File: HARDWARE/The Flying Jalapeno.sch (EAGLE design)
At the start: 97 parts, among them Q2 MMBT2222A, Q3 NDP6020P, Q4 MMBT2222A, Q5 NDP6020P, Q6 BSS138, 200mA/50V, Q7 BSS138, 200mA/50V, U1 ATMEGA2560AU, U2 LM1117, U3 LM1117, U4 LM1117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

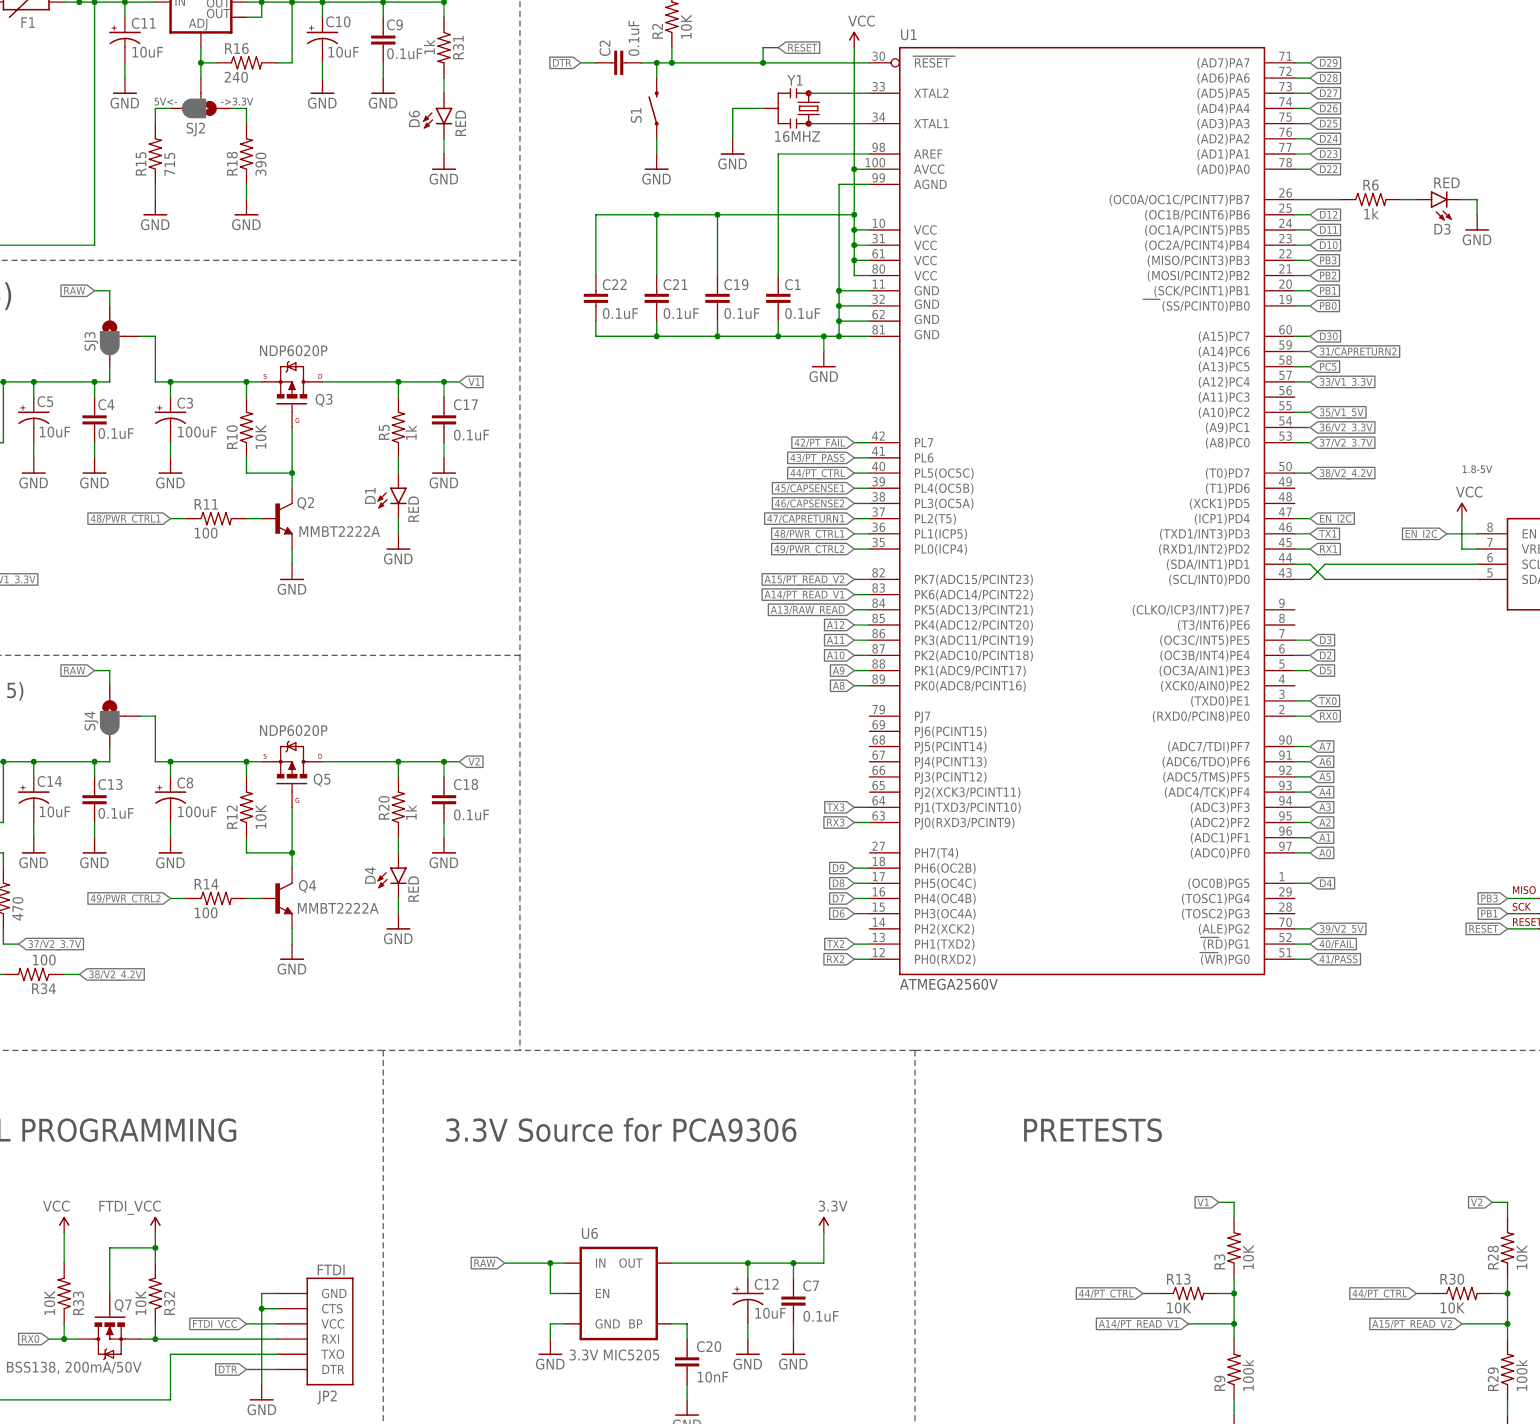
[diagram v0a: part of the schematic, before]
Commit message: update red leds to correct part/prod_ids
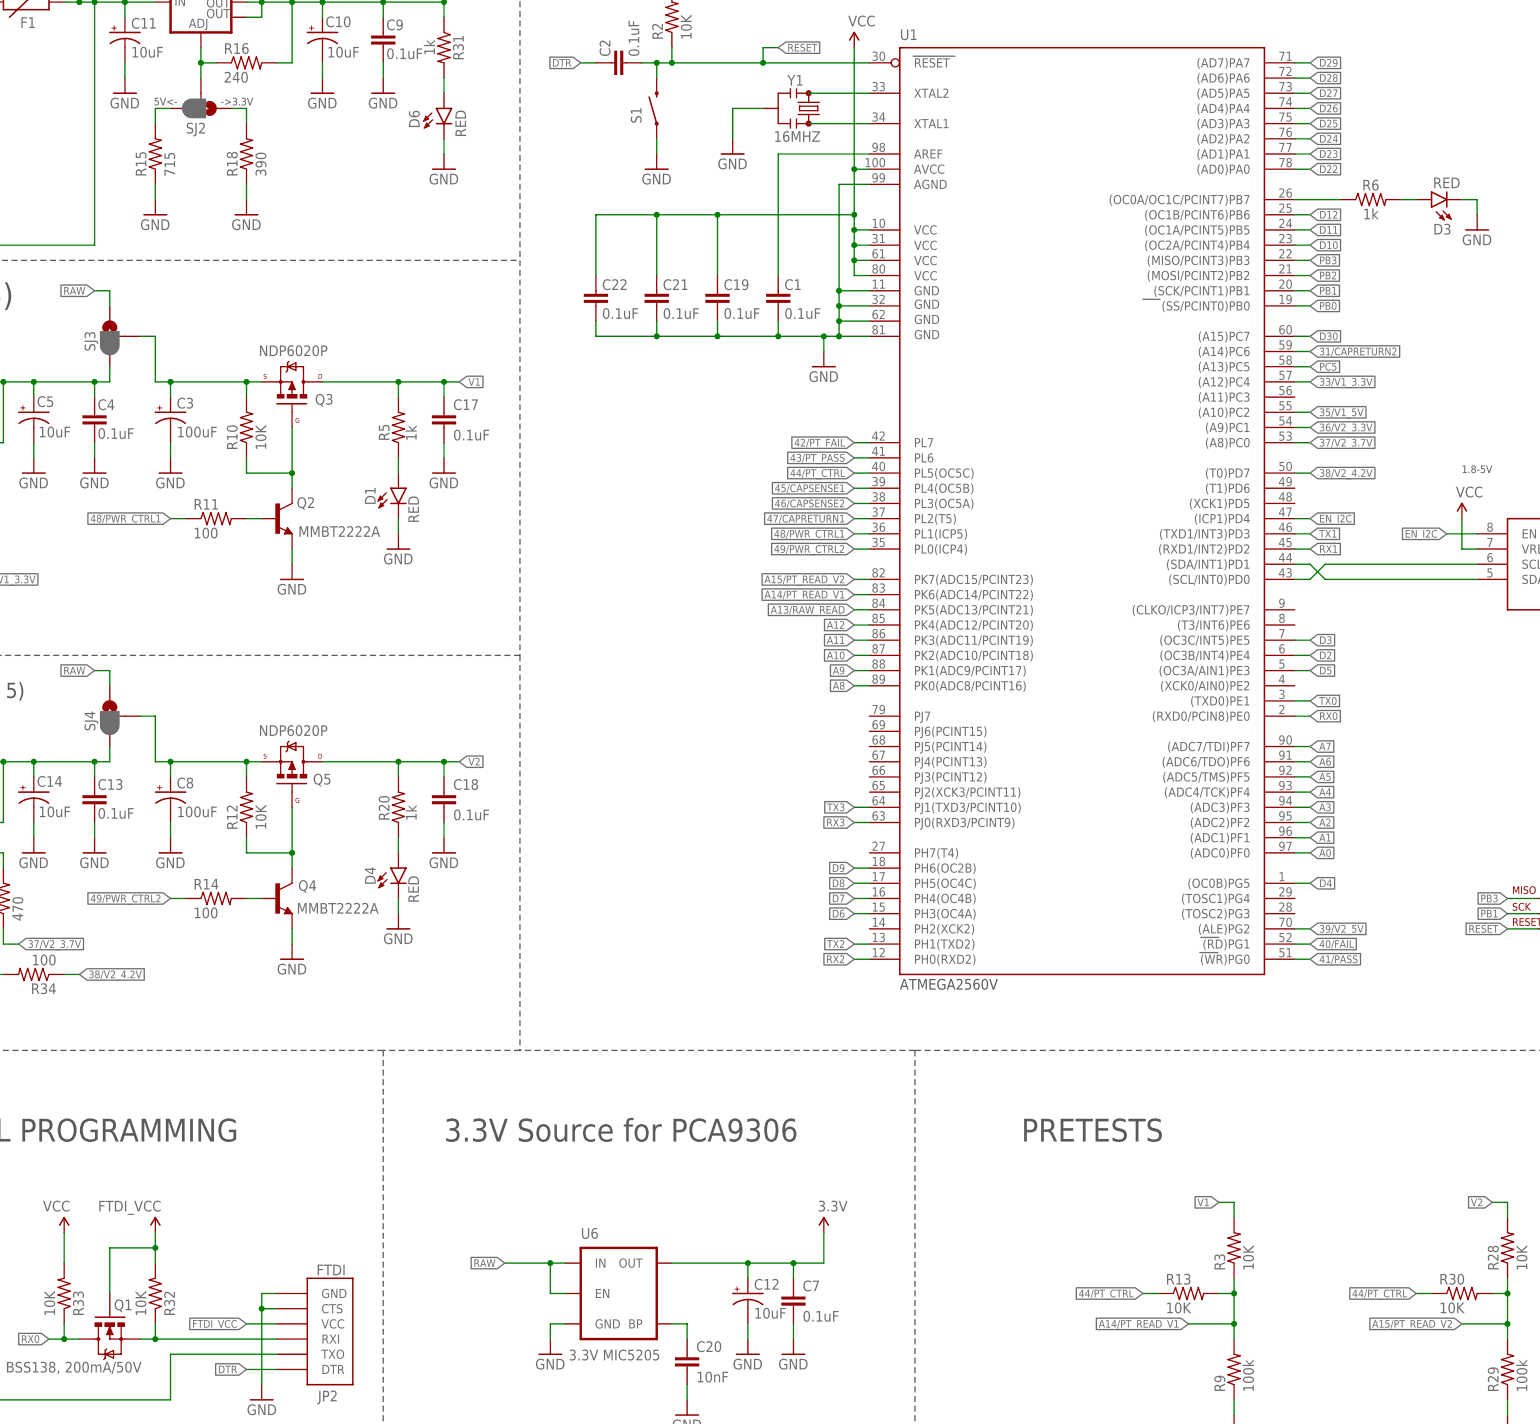
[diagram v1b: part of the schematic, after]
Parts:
- renumbered Q7 to Q1
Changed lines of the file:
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@@
 <part name="P+1" library="SparkFun" deviceset="VCC" device="" value="FTDI_VCC"/>
 <part name="P+4" library="SparkFun" deviceset="VCC" device="" value="VCC"/>
-<part name="Q7" library="SparkFun-DiscreteSemi" deviceset="MOSFET-NCHANNEL" device="BSS138" value="BSS138, 200mA/50V"/>
+<part name="Q1" library="SparkFun-DiscreteSemi" deviceset="MOSFET-NCHANNEL" device="BSS138" value="BSS138, 200mA/50V"/>
 <part name="P+2" library="SparkFun" deviceset="VCC" device="" value="FTDI_VCC"/>
 <part name="P+3" library="SparkFun" deviceset="VCC" device="" value="VCC"/>
@@
 <instance part="P+1" gate="1" x="30.48" y="45.72" rot="MR0"/>
 <instance part="P+4" gate="1" x="15.24" y="45.72" rot="MR0"/>
-<instance part="Q7" gate="G$1" x="53.34" y="38.1" smashed="yes" rot="MR270">
+<instance part="Q1" gate="G$1" x="53.34" y="38.1" smashed="yes" rot="MR270">
 <attribute name="NAME" x="57.15" y="42.926" size="1.778" layer="95" rot="MR0"/>
 <attribute name="VALUE" x="58.674" y="32.512" size="1.778" layer="96" rot="MR0"/>
@@
 <wire x1="45.72" y1="40.64" x2="45.72" y2="38.1" width="0.1524" layer="91"/>
 <junction x="45.72" y="38.1"/>
-<pinref part="Q7" gate="G$1" pin="D"/>
+<pinref part="Q1" gate="G$1" pin="D"/>
 <label x="43.18" y="38.1" size="1.27" layer="95" rot="MR0" xref="yes"/>
 <pinref part="R33" gate="G$1" pin="1"/>
@@
 <junction x="60.96" y="53.34"/>
 <pinref part="P+2" gate="1" pin="VCC"/>
-<pinref part="Q7" gate="G$1" pin="G"/>
+<pinref part="Q1" gate="G$1" pin="G"/>
 <pinref part="R32" gate="G$1" pin="2"/>
 </segment>
@@
 <net name="N$16" class="0">
 <segment>
-<pinref part="Q7" gate="G$1" pin="S"/>
+<pinref part="Q1" gate="G$1" pin="S"/>
 <wire x1="58.42" y1="38.1" x2="60.96" y2="38.1" width="0.1524" layer="91"/>
 <pinref part="R32" gate="G$1" pin="1"/>

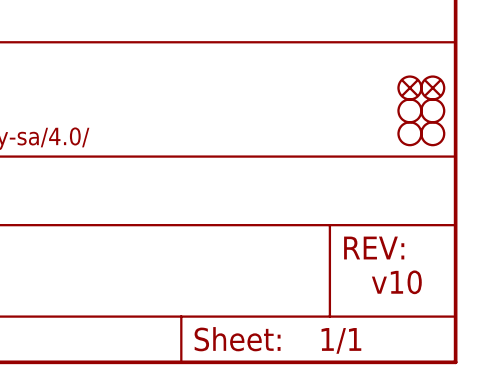
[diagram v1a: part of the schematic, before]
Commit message: changed version to v11, to keep things straight.
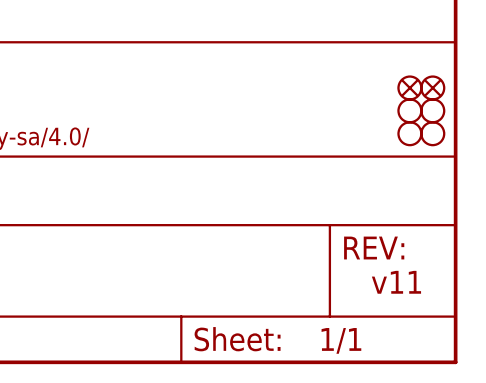
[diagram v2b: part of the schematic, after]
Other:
- note added: "v11"
- note removed: "v10"
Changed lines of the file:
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@@
 <text x="127" y="271.78" size="3.81" layer="97">MICRO</text>
 <text x="354.33" y="11.43" size="2.54" layer="94">Pete Lewis</text>
-<text x="422.402" y="7.62" size="2.54" layer="94">v10</text>
+<text x="422.402" y="7.62" size="2.54" layer="94">v11</text>
 <text x="185.42" y="96.52" size="1.778" layer="97">ATMEGA2560V</text>
 <text x="337.82" y="264.16" size="3.81" layer="97">2x30 RA connector to testbeds</text>

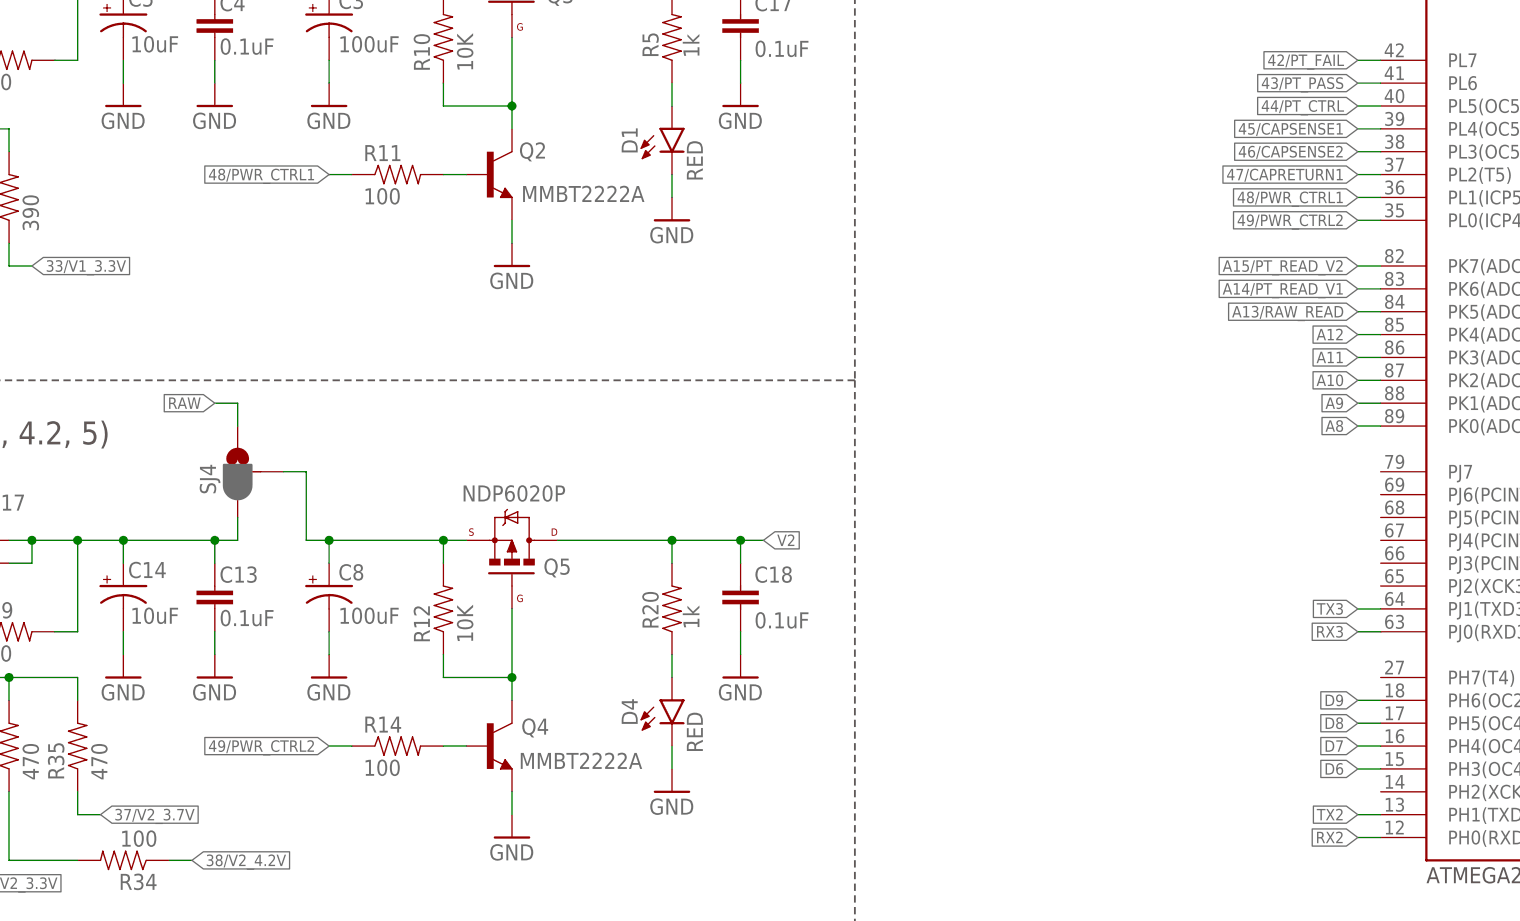
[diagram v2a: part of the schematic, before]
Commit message: cleaning up net naming convention on 48/49
"48/PWR_CTRL_V1" and "49/PWR_CTRL_V2".

issue #3
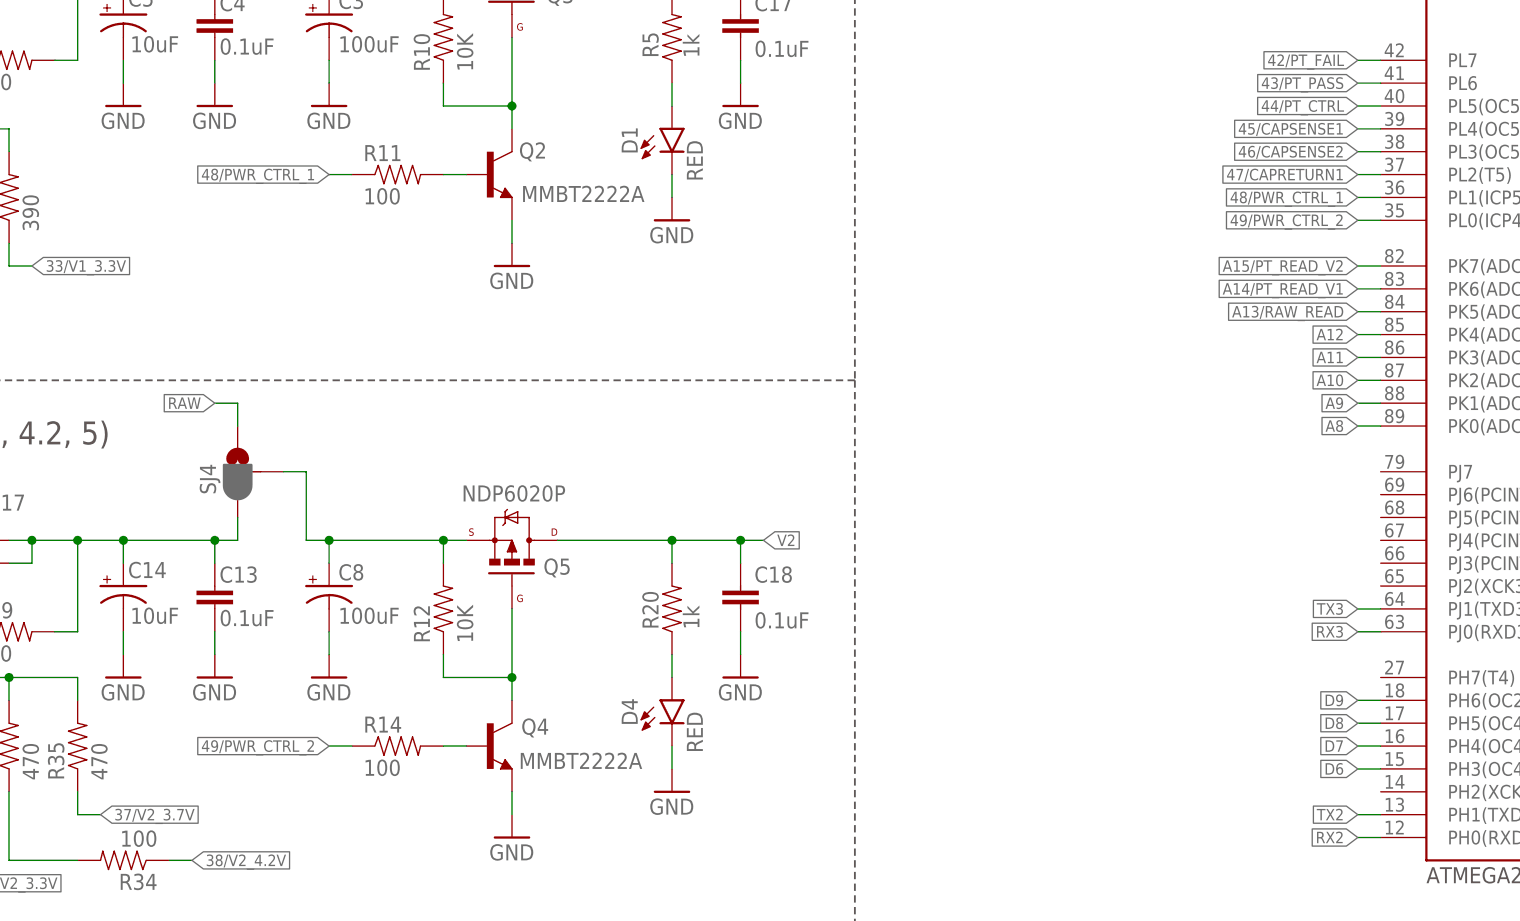
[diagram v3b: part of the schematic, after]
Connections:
- net 48/PWR_CTRL1 renamed 48/PWR_CTRL_1
- net 49/PWR_CTRL2 renamed 49/PWR_CTRL_2
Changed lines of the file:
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@@
 </segment>
 </net>
-<net name="48/PWR_CTRL1" class="0">
+<net name="48/PWR_CTRL_1" class="0">
 <segment>
 <pinref part="R11" gate="G$1" pin="1"/>
@@
 </segment>
 </net>
-<net name="49/PWR_CTRL2" class="0">
+<net name="49/PWR_CTRL_2" class="0">
 <segment>
 <pinref part="R14" gate="G$1" pin="1"/>
